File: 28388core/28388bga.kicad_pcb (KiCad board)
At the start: 2 copper layers, 276 parts, among them IC1 F28388DZWTS, IC2 TPS62420DRCT, IC6 OPA4350EA_250, IC7 TPS3702CX33DDCT, IC8 CDCLVC1104PW, IC9 TPS3702CX12DDCT, J1 Conn_01x02, J9 Conn_02x07_Odd_Even, Q1 FMMT618TA, Q11 AT24C16C-SSHM-T, Q13 DP83822IRHBR, Q14 DP83822IRHBR, Q2 FMMT618TA, Q4 FMMT618TA, Q46 TYPEC-304-ACP16, Q7 FMMT618TA, SW1 SW_DIP_x02, SW2 SW_Push, U1 ADR423ARMZ, Y1 ECS-2520S33-250-FN-TR

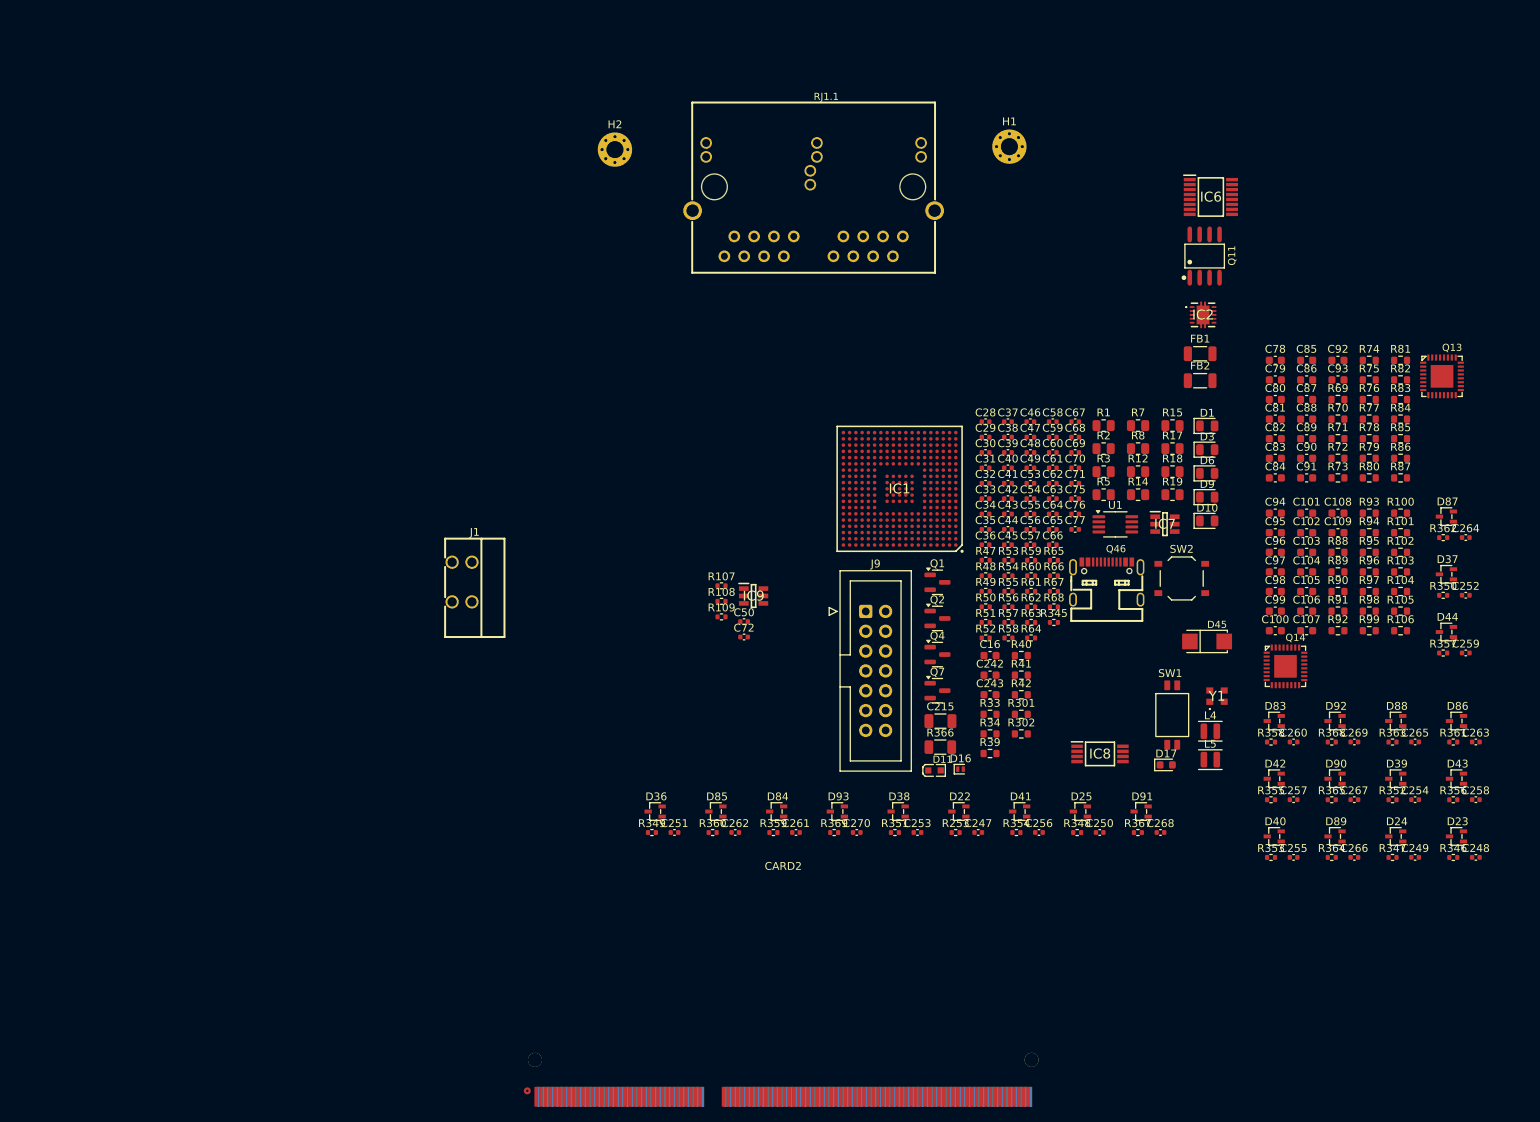
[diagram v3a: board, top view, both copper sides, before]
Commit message: 1. usb 稳压、防倒灌 1 2. 仿真器贴片 1 3. EtherCAT确认 1 4. EtherCAT差分信号 5. 金手指选型换1.6 要不就1.0？
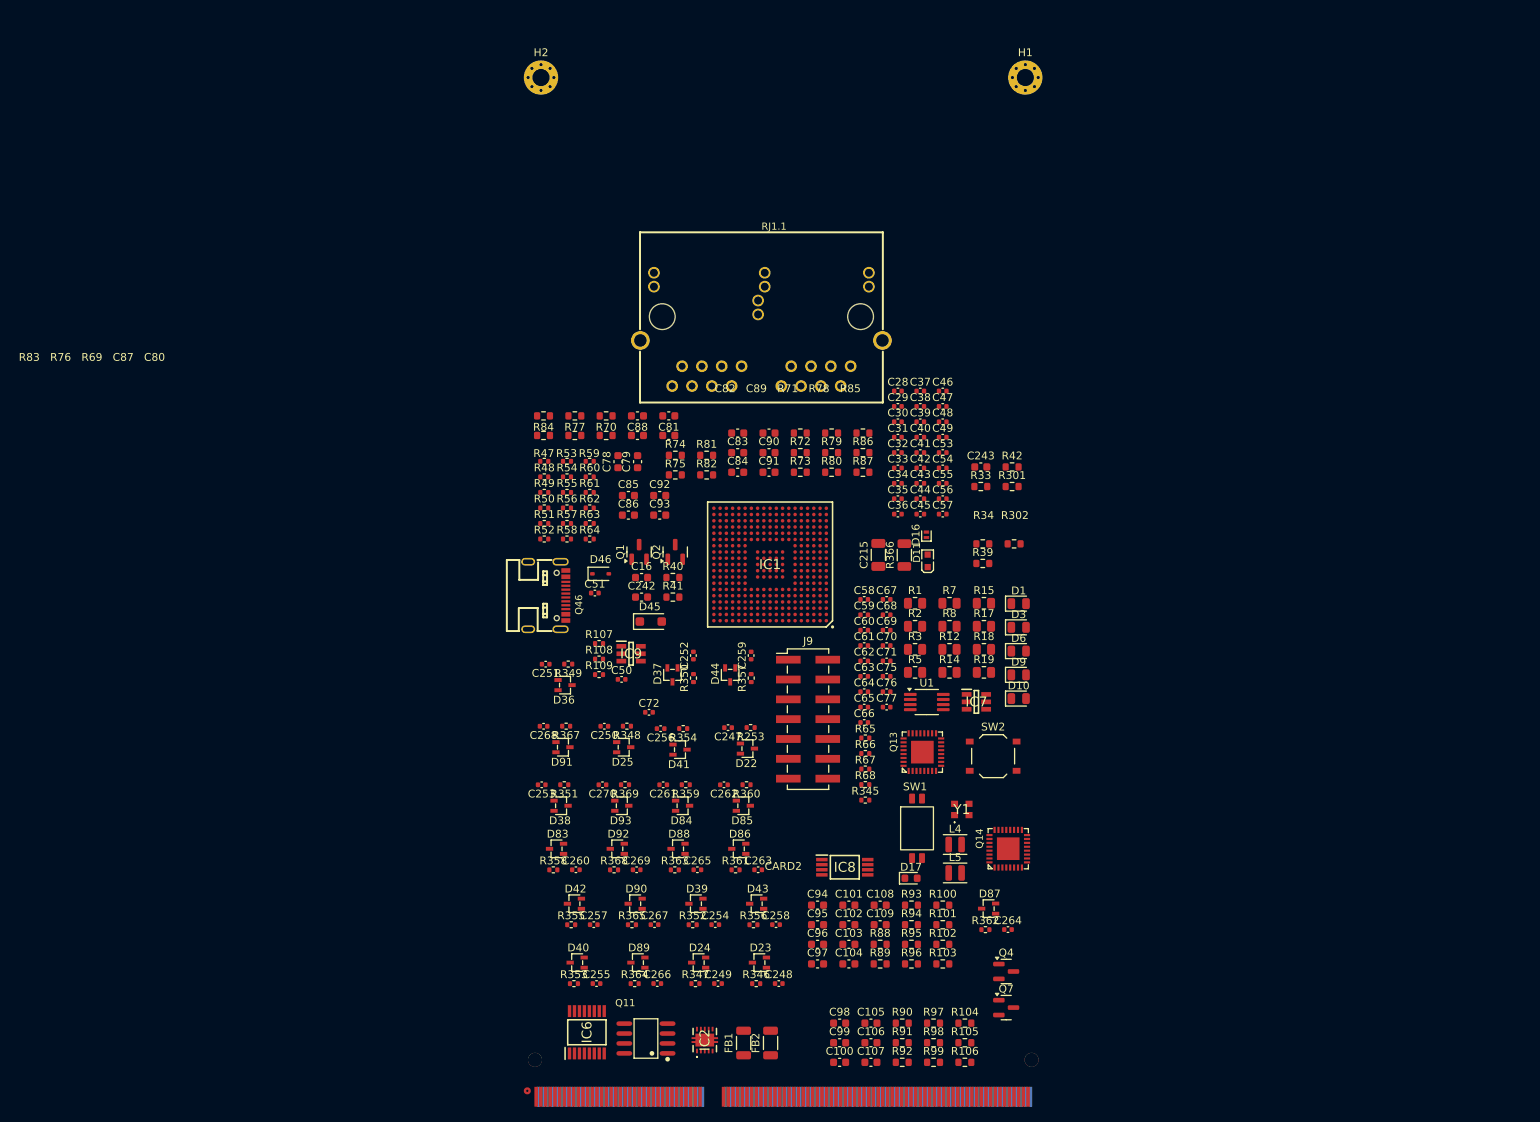
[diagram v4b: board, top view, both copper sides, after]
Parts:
- removed J1: Conn_01x02, 1mmlab_footprint:CONN-TH_2P-P2.54_DIBO_DB141R-2.54-2P
- added C51: 22uF, Capacitor_SMD:C_0402_1005Metric, F.Cu at (140.2, 93.3)
- added D46: SD15, Diode_SMD:D_SOD-323, F.Cu at (141.0, 90.8)
- D45: value SK36A-LTP -> PMEG2010EH; footprint Lib_sheet_10:SMA_L4.3-W2.6-LS5.2-RD -> Diode_SMD:D_SOD-123F
- J9: footprint Connector_IDC:IDC-Header_2x07_P2.54mm_Vertical -> Connector_PinHeader_2.54mm:PinHeader_2x07_P2.54mm_Vertical_SMD
- moved IC6 133.5 mm to (139.2, 149.6), turned to 90 degrees
- moved Q11 123.1 mm to (146.8, 150.4), turned to 90 degrees
- moved IC2 112.7 mm to (154.3, 150.6), turned to 90 degrees
- moved R83 109.9 mm to (133.7, 73.1), turned to 180 degrees
- moved R84 109.8 mm to (133.7, 70.6), turned to 180 degrees
- moved FB1 105.9 mm to (159.3, 150.9), turned to 90 degrees
- moved R76 101.8 mm to (137.7, 73.1), turned to 180 degrees
- moved R77 101.7 mm to (137.7, 70.6), turned to 180 degrees
- moved FB2 101.1 mm to (162.8, 150.9), turned to 90 degrees
- moved D37 100.0 mm to (150.2, 103.8), turned to 90 degrees
- moved C252 99.2 mm to (152.9, 101.3), turned to 90 degrees
- moved R350 96.6 mm to (152.9, 104.2), turned to 90 degrees
- moved R69 93.8 mm to (141.7, 73.1), turned to 180 degrees
- moved R70 93.7 mm to (141.7, 70.6), turned to 180 degrees
- moved C260 93.4 mm to (137.8, 128.8)
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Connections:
- net Net-(Q13-RD_M) renamed /RD1-
- net Net-(Q13-RD_P) renamed /RD1+
- net Net-(Q13-TD_M) renamed /TD1-
- net Net-(Q13-TD_P) renamed /TD1+
- net Net-(Q14-RD_M) renamed /RD2-
- net Net-(Q14-RD_P) renamed /RD2+
- net Net-(Q14-TD_M) renamed /TD2-
- net Net-(Q14-TD_P) renamed /TD2+
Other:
- copper layers 2 -> 4

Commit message: 分组后分配引脚
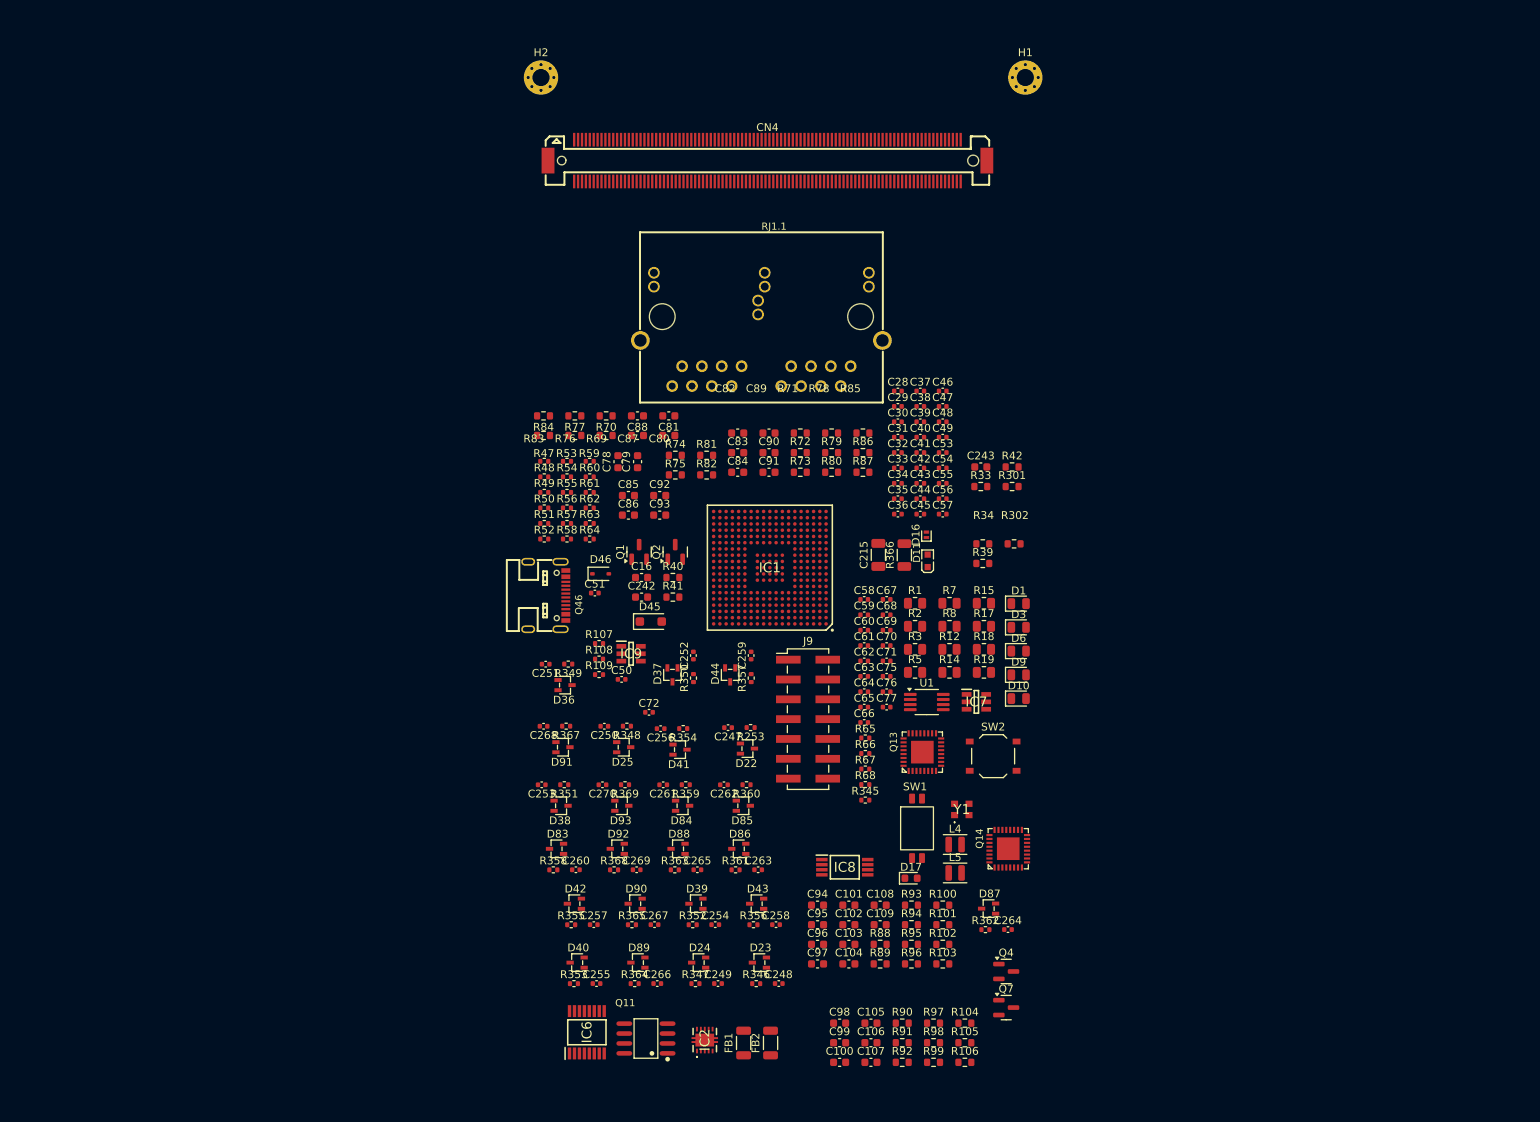
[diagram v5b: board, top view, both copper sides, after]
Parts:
- removed CARD2: DDR3, 1mmlab_footprint:PCBComponent_1 - duplicate
- added CN4: ~, 1mmlab_footprint:CONN-SMD_200P-P0.50_X0510WVS-200AS-LPV01, F.Cu at (162.3, 37.9)
- moved IC1 0.41 mm to (162.7, 90.1)
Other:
- board outline added: 53.9 x 1.4 mm

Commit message: 使用4个50PIN引脚，通常按照337封装分配位置
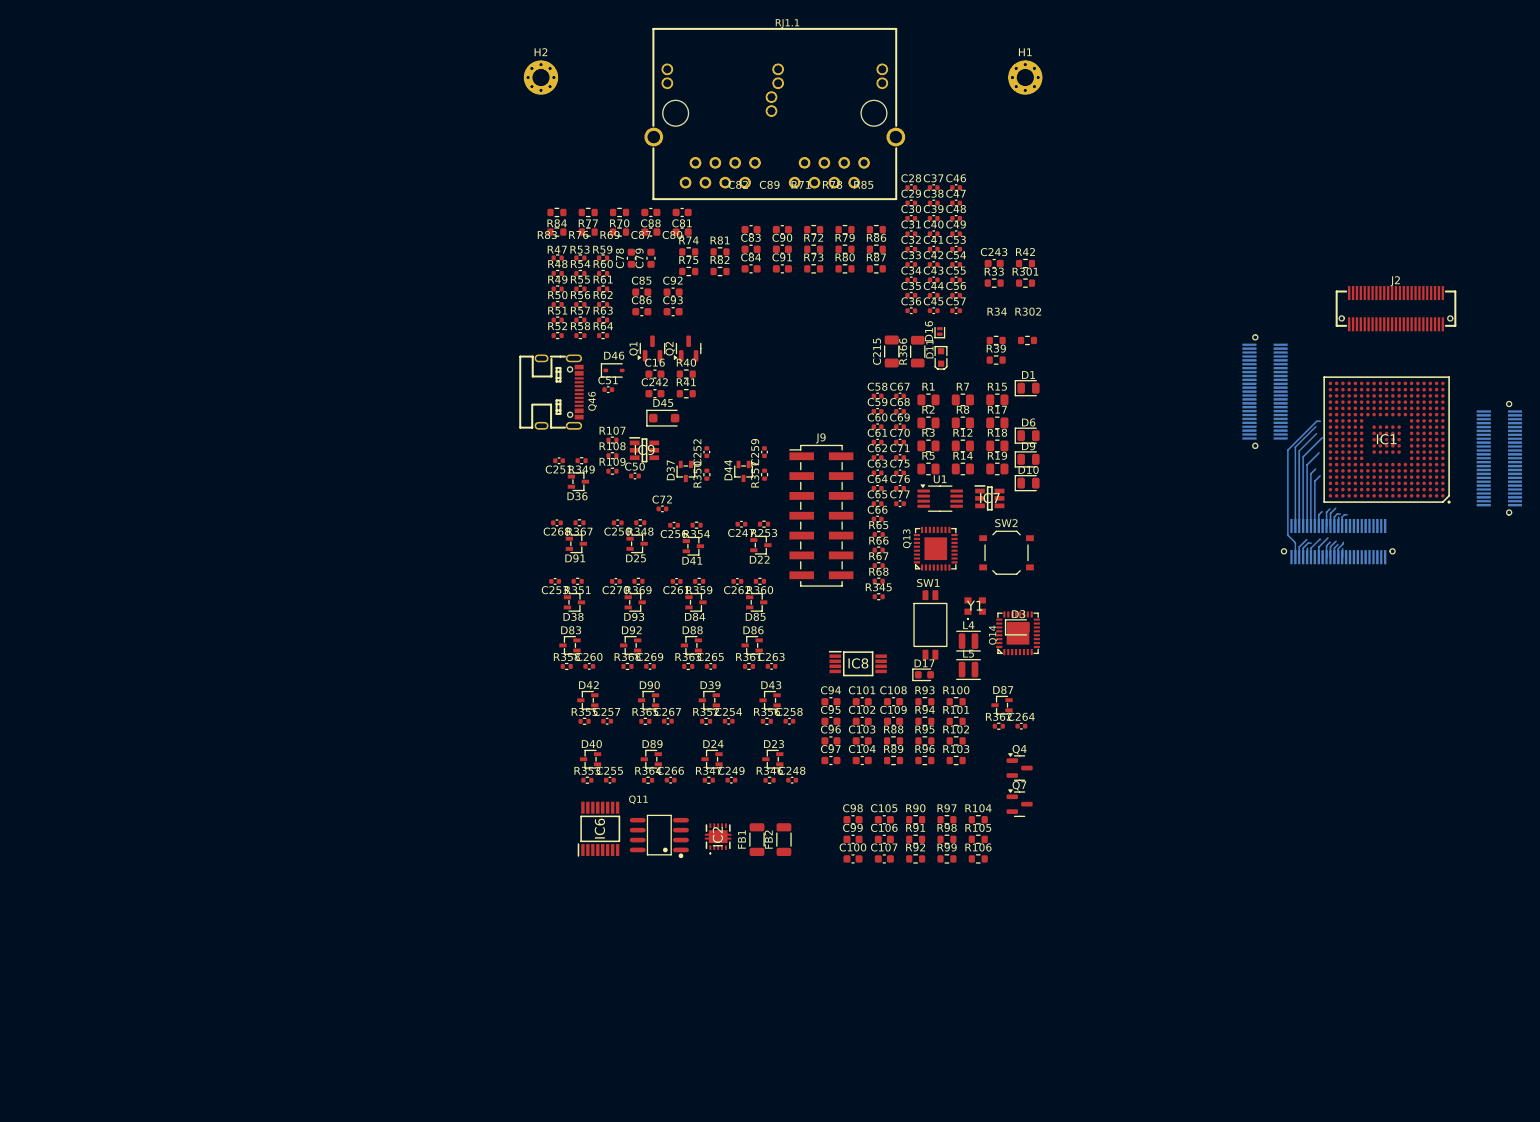
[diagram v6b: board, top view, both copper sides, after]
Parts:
- removed CN4: ~, 1mmlab_footprint:CONN-SMD_200P-P0.50_X0510WVS-200AS-LPV01
- added J2: ~, 1mmlab_footprint:CONN-SMD_50P-P0.50_XKB_X0515WVS-50AS-9TV01, F.Cu at (242.8, 56.9)
- added J3: ~, 1mmlab_footprint:CONN-SMD_50P-P0.50_XKB_X0515WVS-50AS-9TV01, B.Cu at (256.1, 76.0)
- added J4: ~, 1mmlab_footprint:CONN-SMD_50P-P0.50_XKB_X0515WVS-50AS-9TV01, B.Cu at (235.5, 86.7)
- added J5: ~, 1mmlab_footprint:CONN-SMD_50P-P0.50_XKB_X0515WVS-50AS-9TV01, B.Cu at (226.1, 67.5)
- moved IC1 80.7 mm to (241.7, 73.7)
- moved D1 27.6 mm to (195.8, 67.1)
- moved D10 27.6 mm to (195.8, 79.2)
- moved D6 27.6 mm to (195.8, 73.2)
- moved D9 27.6 mm to (195.8, 76.2)
- moved Q14 27.6 mm to (194.4, 98.5)
- moved C101 26.1 mm to (174.5, 107.2)
- moved C104 26.1 mm to (174.5, 114.8)
- moved C106 26.1 mm to (177.3, 124.8)
- moved C108 26.1 mm to (178.5, 107.2)
- moved C250 26.1 mm to (143.2, 84.3)
- moved C251 26.1 mm to (135.7, 76.4)
- moved C253 26.1 mm to (135.2, 91.8)
- moved C261 26.1 mm to (150.7, 91.8)
- moved C262 26.1 mm to (158.5, 91.8)
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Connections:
- IC1 pad A11: /GPIO84 -> /ESC_TX0_EN
- IC1 pad A12: /ESC_MDIO -> /GPIO153
- IC1 pad A13: /ESC_PHY1 -> /GPIO149
- IC1 pad A14: /GPIO81 -> /ESC_RX0_D1
- IC1 pad A15: /GPIO77 -> /ESC_RX0_CLK
- IC1 pad A16: /GPIO73 -> /ESC_TX1_D2
- IC1 pad A17: /GPIO70 -> /ESC_RX1_DV
- IC1 pad A8: /ESC_RX0_CLK -> /GPIO163
- IC1 pad B10: /ESC_TX0_CLK -> /GPIO157
- IC1 pad B11: /GPIO85 -> /ESC_TX0_CLK
- IC1 pad B14: /GPIO82 -> /ESC_RX0_D2
- IC1 pad B15: /GPIO78 -> /ESC_RX0_DV
- IC1 pad B16: /GPIO72 -> /ESC_TX1_D3
- IC1 pad B17: /GPIO71 -> /ESC_RX1_ERR
- IC1 pad B18: /GPIO69 -> /ESC_RX1_CLK
- IC1 pad B8: /ESC_RX0_ERR -> /GPIO164
- IC1 pad C10: /ESC_TX0_D0 -> /GPIO158
- IC1 pad C12: /ESC_RESET -> /GPIO155
- IC1 pad C14: /GPIO83 -> /ESC_RX0_D3
- IC1 pad C15: /GPIO79 -> /ESC_RX0_ERR
- IC1 pad C16: /GPIO76 -> /ESC_RESET
- IC1 pad C17: /GPIO74 -> /ESC_TX1_D1
- IC1 pad C18: /GPIO68 -> /ESC_PHY1
- IC1 pad C4: /ESC_RX0_D2 -> /GPIO167
- IC1 pad C5: /ESC_RX0_D0 -> /GPIO165
- IC1 pad D11: /GPIO87 -> /ESC_TX0_D0
- IC1 pad D12: /ESC_TX0_EN -> /GPIO156
- IC1 pad D13: /ESC_MDC -> /GPIO152
- IC1 pad D15: /GPIO80 -> /ESC_RX0_D0
- IC1 pad D16: /GPIO75 -> /ESC_TX1_D0
- IC1 pad D4: /ESC_RX0_D3 -> /GPIO168
- IC1 pad D5: /ESC_RX0_D1 -> /GPIO166
- IC1 pad D9: /ESC_RX0_DV -> /GPIO162
- IC1 pad E18: /GPIO47 -> /ESC_MDIO
- IC1 pad E19: /GPIO46 -> /ESC_MDC
- IC1 pad J16: /GPIO63 -> /ESC_RX1_D0
- IC1 pad K16: /GPIO65 -> /ESC_RX1_D2
- IC1 pad K17: /GPIO66 -> /ESC_RX1_D3
- IC1 pad K18: /GPIO44 -> /ESC_TX1_CLK
- IC1 pad K19: /GPIO45 -> /ESC_TX1_EN
- IC1 pad L17: /GPIO64 -> /ESC_RX1_D1
- IC1 pad L19: /ESC_RX1_D3 -> /GPIO142
- IC1 pad M18: /ESC_RX1_D2 -> /GPIO141
- IC1 pad M19: /ESC_RX1_D1 -> /GPIO140
- IC1 pad N19: /ESC_RX1_D0 -> /GPIO139
- IC1 pad T10: /ESC_TX1_EN -> /GPIO129
- IC1 pad T17: /ESC_RX1_DV -> /GPIO136
- IC1 pad T18: /ESC_RX1_CLK -> /GPIO137
- IC1 pad T19: /ESC_RX1_ERR -> /GPIO138
- IC1 pad U10: /ESC_TX1_CLK -> /GPIO130
- IC1 pad U18: /ESC_TX1_D3 -> /GPIO135
- IC1 pad V10: /ESC_TX1_D0 -> /GPIO131
- IC1 pad V18: /ESC_TX1_D2 -> /GPIO134
- IC1 pad W18: /ESC_TX1_D1 -> /GPIO132
- R47 pad 2: /GPIO84 -> /ESC_TX0_EN
- R49 pad 2: /GPIO72 -> /ESC_TX1_D3
- SW1 pad 1: /GPIO72 -> /ESC_TX1_D3
- SW1 pad 2: /GPIO84 -> /ESC_TX0_EN
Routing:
- net /GPIO57: track 0.00 -> 19.8 mm
- net /GPIO56: track 0.00 -> 13.8 mm
- net /GPIO142: track 0.00 -> 12.7 mm
- net /GPIO141: track 0.00 -> 12.3 mm
- net /GPIO61: track 0.00 -> 9.99 mm
- net /GPIO59: track 0.00 -> 7.53 mm
- net /GPIO133: track 0.00 -> 6.69 mm
- net /GPIO42: track 0.00 -> 2.94 mm
- net /GPIO62: track 0.00 -> 2.84 mm
- net /GPIO140: track 0.00 -> 2.67 mm
- net /GPIO156: track 0.00 -> 2.55 mm
- net /GPIO139: track 0.00 -> 2.43 mm
- net /GPIO147: track 0.00 -> 2.37 mm
- net /GPIO154: track 0.00 -> 2.33 mm
- net /GPIO86: track 0.00 -> 2.18 mm
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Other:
- board size 53.9 x 1.4 mm -> 14.5 x 0.6 mm
